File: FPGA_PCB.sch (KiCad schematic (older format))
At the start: 18 parts, among them J1 M3498-99, J10 Conn_Coaxial, J11 Conn_Coaxial, J12 Conn_01x03_Male, J13 Conn_01x03_Male, J2 M3498-99, J3 M3498-99, J4 M3498-99, J5 Conn_01x04_Male, J6 Conn_01x04_Male, J7 Conn_01x04_Male, J8 Conn_01x04_Male, J9 Conn_01x04_Male, SW1 SW_Push, U1 CPG08462

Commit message: Add files via upload
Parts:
- J1, J2, J3, J4: symbol M3498-99:M3498-99 -> FPGA_PCB-rescue:M3498-99-M3498-99
- SW1: footprint (none) -> Button_Switch_SMD:SW_SPST_TL3305A; Digikey link (none) -> https://www.digikey.com/en/products/detail/e-switch/TL3305A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
- U1: footprint (none) -> 18726-PCB-master:CPG08462_original
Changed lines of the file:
@@
 EESchema Schematic File Version 4
-LIBS:FPGA_PCB-cache
 EELAYER 30 0
 EELAYER END
@@
 F 0 "U1" H 3850 3750 60  0000 L CNN
 F 1 "CPG08462" H 3850 3650 60  0000 L CNN
-F 2 "" H 3750 3700 60  0000 C CNN
+F 2 "18726-PCB-master:CPG08462_original" H 3750 3700 60  0000 C CNN
 F 3 "" H 3750 3700 60  0000 C CNN
 	1    3750 3600
@@
 VSS
 $Comp
-L M3498-99:M3498-99 J1
+L FPGA_PCB-rescue:M3498-99-M3498-99 J1
 U 1 1 6165D330
 P 4000 6300
@@
 $EndComp
 $Comp
-L M3498-99:M3498-99 J3
+L FPGA_PCB-rescue:M3498-99-M3498-99 J3
 U 1 1 6165F6EF
 P 5950 6300
@@
 $EndComp
 $Comp
-L M3498-99:M3498-99 J4
+L FPGA_PCB-rescue:M3498-99-M3498-99 J4
 U 1 1 6166863E
 P 5950 7250
@@
 F 0 "SW1" H 10200 4685 50  0000 C CNN
 F 1 "SW_Push" H 10200 4594 50  0000 C CNN
-F 2 "" H 10200 4600 50  0001 C CNN
+F 2 "Button_Switch_SMD:SW_SPST_TL3305A" H 10200 4600 50  0001 C CNN
 F 3 "~" H 10200 4600 50  0001 C CNN
+F 4 "https://www.digikey.com/en/products/detail/e-switch/TL3305AF260QG/5816184" H 10200 4400 50  0001 C CNN "Digikey link"
 	1    10200 4400
 	1    0    0    -1
@@
 	3500 7250 4000 7250
 $Comp
-L M3498-99:M3498-99 J2
+L FPGA_PCB-rescue:M3498-99-M3498-99 J2
 U 1 1 6166408E
 P 4000 7250

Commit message: sch done
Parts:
- removed J1, J2, J3, J4: M3498-99, M3498-99:M3498-99, symbol FPGA_PCB-rescue:M3498-99-M3498-99
- added J1, J14, J15, J18, J19, J2: Conn_01x01_Male, Connector_PinHeader_2.54mm:PinHeader_1x01_P2.54mm_Vertical, symbol Connector:Conn_01x01_Male
- added J16, J17, J3, J4: 73096-2, 73096-2:73096-2, symbol 73096-2:73096-2
- added J20: Conn_01x01_Male, symbol Connector:Conn_01x01_Male
- J12, J13: footprint (none) -> Connector_PinHeader_2.54mm:PinHeader_1x03_P2.54mm_Vertical
- J5, J6, J7, J8, J9: footprint (none) -> Connector_PinHeader_2.54mm:PinHeader_1x04_P2.54mm_Vertical
- R1: footprint (none) -> Resistor_SMD:R_0805_2012Metric_Pad1.15x1.40mm_HandSolder
- U1: footprint 18726-PCB-master:CPG08462_original -> CPG08462:CPG08462_original; symbol FPGA_PCB-rescue:CPG08462-cpg08462 -> CPG08462:CPG08462
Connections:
- wire segments 139 -> 142
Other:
- note added: "in case banana jack is not working"
- moved on the sheet: C1, C2

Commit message: layout done
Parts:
- added H1, H2, H3, H4: MountingHole, MountingHole:MountingHole_3.2mm_M3, symbol Mechanical:MountingHole
- J20: footprint (none) -> Connector_PinHeader_2.54mm:PinHeader_1x01_P2.54mm_Vertical
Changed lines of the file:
@@
 F 0 "J20" H 9758 5181 50  0000 C CNN
 F 1 "Conn_01x01_Male" H 9758 5090 50  0000 C CNN
-F 2 "" H 9650 5000 50  0001 C CNN
+F 2 "Connector_PinHeader_2.54mm:PinHeader_1x01_P2.54mm_Vertical" H 9650 5000 50  0001 C CNN
 F 3 "~" H 9650 5000 50  0001 C CNN
 	1    9650 5000
@@
 Text Label 10200 5000 0    50   ~ 0
 RST
+$Comp
+L Mechanical:MountingHole H1
+U 1 1 615A752D
+P 5600 950
+F 0 "H1" H 5700 996 50  0000 L CNN
+F 1 "MountingHole" H 5700 905 50  0000 L CNN
+F 2 "MountingHole:MountingHole_3.2mm_M3" H 5600 950 50  0001 C CNN
+F 3 "~" H 5600 950 50  0001 C CNN
+	1    5600 950
+	1    0    0    -1
+$EndComp
+$Comp
+L Mechanical:MountingHole H2
+U 1 1 615A7BC1
+P 5600 1300
+F 0 "H2" H 5700 1346 50  0000 L CNN
+F 1 "MountingHole" H 5700 1255 50  0000 L CNN
+F 2 "MountingHole:MountingHole_3.2mm_M3" H 5600 1300 50  0001 C CNN
+F 3 "~" H 5600 1300 50  0001 C CNN
+	1    5600 1300
+	1    0    0    -1
+$EndComp
+$Comp
+L Mechanical:MountingHole H3
+U 1 1 615AD8DC
+P 6500 950
+F 0 "H3" H 6600 996 50  0000 L CNN
+F 1 "MountingHole" H 6600 905 50  0000 L CNN
+F 2 "MountingHole:MountingHole_3.2mm_M3" H 6500 950 50  0001 C CNN
+F 3 "~" H 6500 950 50  0001 C CNN
+	1    6500 950
+	1    0    0    -1
+$EndComp
+$Comp
+L Mechanical:MountingHole H4
+U 1 1 615B3580
+P 6500 1300
+F 0 "H4" H 6600 1346 50  0000 L CNN
+F 1 "MountingHole" H 6600 1255 50  0000 L CNN
+F 2 "MountingHole:MountingHole_3.2mm_M3" H 6500 1300 50  0001 C CNN
+F 3 "~" H 6500 1300 50  0001 C CNN
+	1    6500 1300
+	1    0    0    -1
+$EndComp
 $EndSCHEMATC

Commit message: ver 2.0
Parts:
- removed J16, J17, J3, J4: 73096-2, 73096-2:73096-2, symbol 73096-2:73096-2
- added C10, C11, C12, C13, C14, C15, C16, C17, C18, C3, C4, C5, C6, C7, C8, C9: 100p, Capacitor_SMD:C_0805_2012Metric_Pad1.15x1.40mm_HandSolder, symbol Device:C
- added J16, J17, J21, J22, J23: Conn_01x04_Male, Connector_PinHeader_2.54mm:PinHeader_1x04_P2.54mm_Vertical, symbol Connector:Conn_01x04_Male
- added J24, J25: Conn_01x01_Male, Connector_PinHeader_2.54mm:PinHeader_1x01_P2.54mm_Vertical, symbol Connector:Conn_01x01_Male
- added J26, J27: Conn_01x03_Male, Connector_PinHeader_2.54mm:PinHeader_1x03_P2.54mm_Vertical, symbol Connector:Conn_01x03_Male
- added J28, J3, J4: Conn_Coaxial, Connector_Coaxial:BNC_TEConnectivity_1478204_Vertical, symbol Connector:Conn_Coaxial
- added JP1, JP2: Jumper_NC_Dual, Connector_PinHeader_2.54mm:PinHeader_1x03_P2.54mm_Vertical, symbol Device:Jumper_NC_Dual
- added U2, U3: SN74LVC8T245DWR, SOIC127P1030X265-24N, symbol SN74LVC8T245DWR:SN74LVC8T245DWR
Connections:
- net labels added: 3.3V, clb_scan_en_3.3, clb_scan_in_3.3, clb_scan_out_3.3, conn_scan_en_3.3, conn_scan_in_3.3, conn_scan_out_3.3
- wire segments 142 -> 269
- no-connect marks 47 -> 67
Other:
- note removed: "in case banana jack is not working"
- moved on the sheet: C1, C2, J1, J12, J13, J14, J2, J20, J5, J6, J7, J8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

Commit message: ver 3.0: added i/o level shifters
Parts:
- added JP7: Jumper_NC_Dual, Connector_PinHeader_2.54mm:PinHeader_1x03_P2.54mm_Vertical, symbol Device:Jumper_NC_Dual
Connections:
- net labels added: RST_header, RST_switch
- wire segments 269 -> 275
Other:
- moved on the sheet: C1, C10, C11, C12, C13, C14, C15, C16, C17, C18, C2, C3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

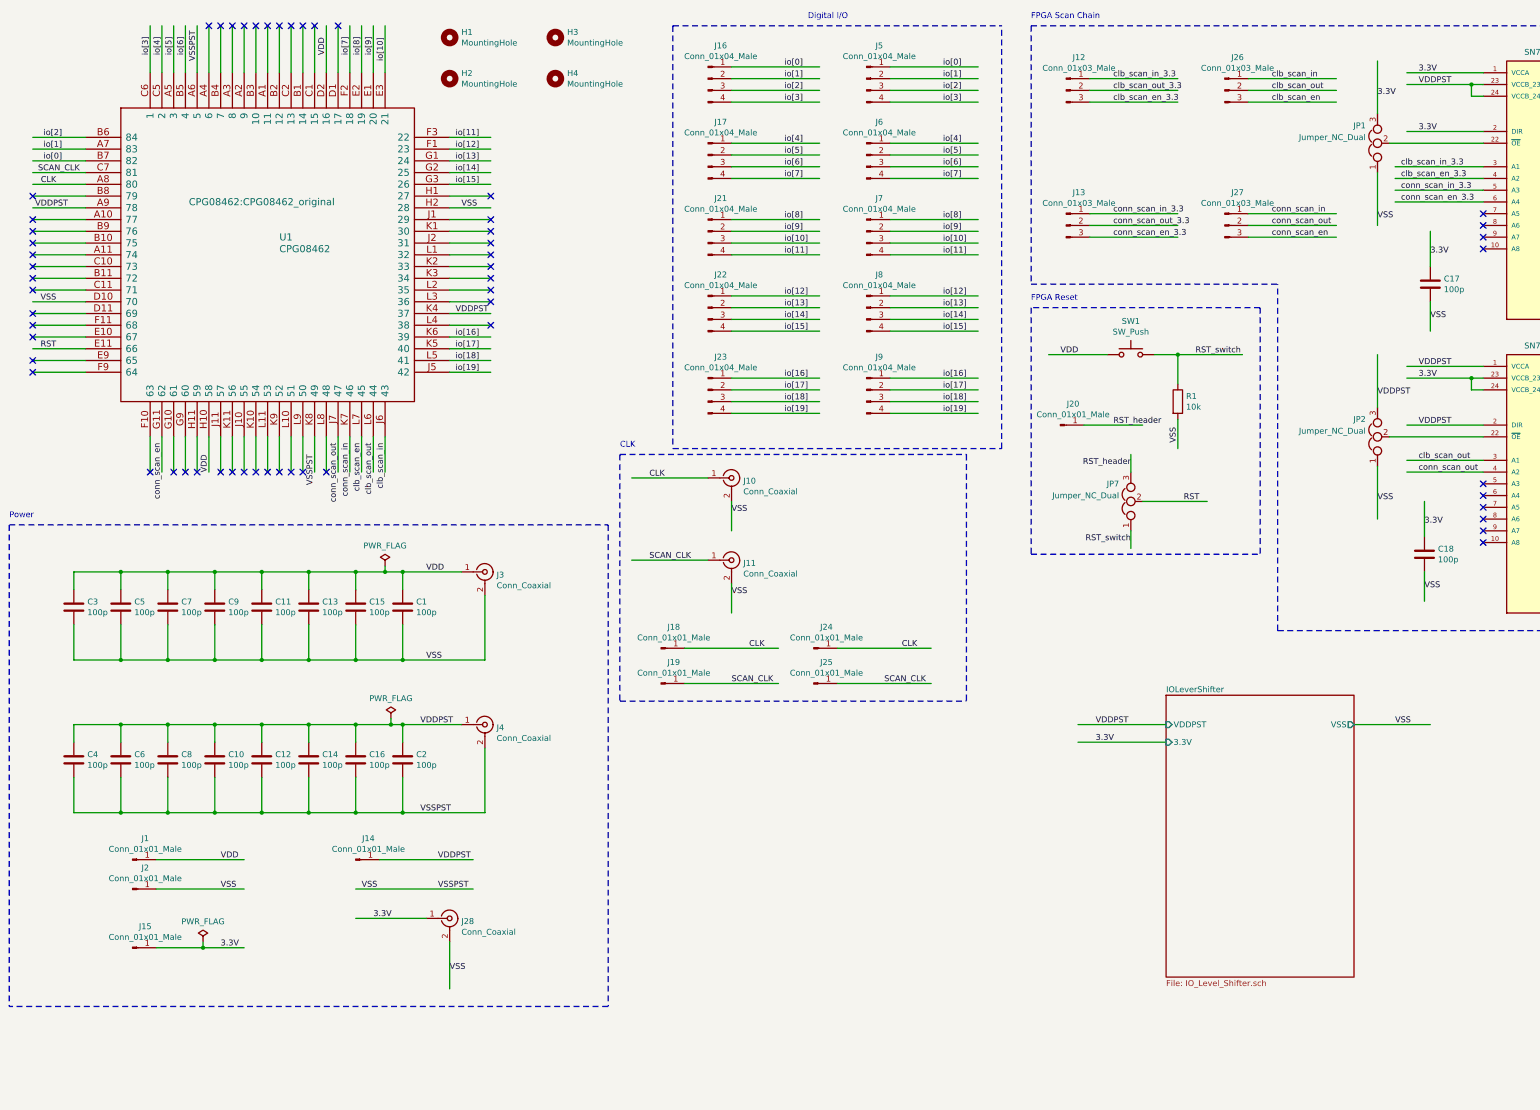
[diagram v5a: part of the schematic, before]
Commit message: ver 4.0: added 1.8V pin
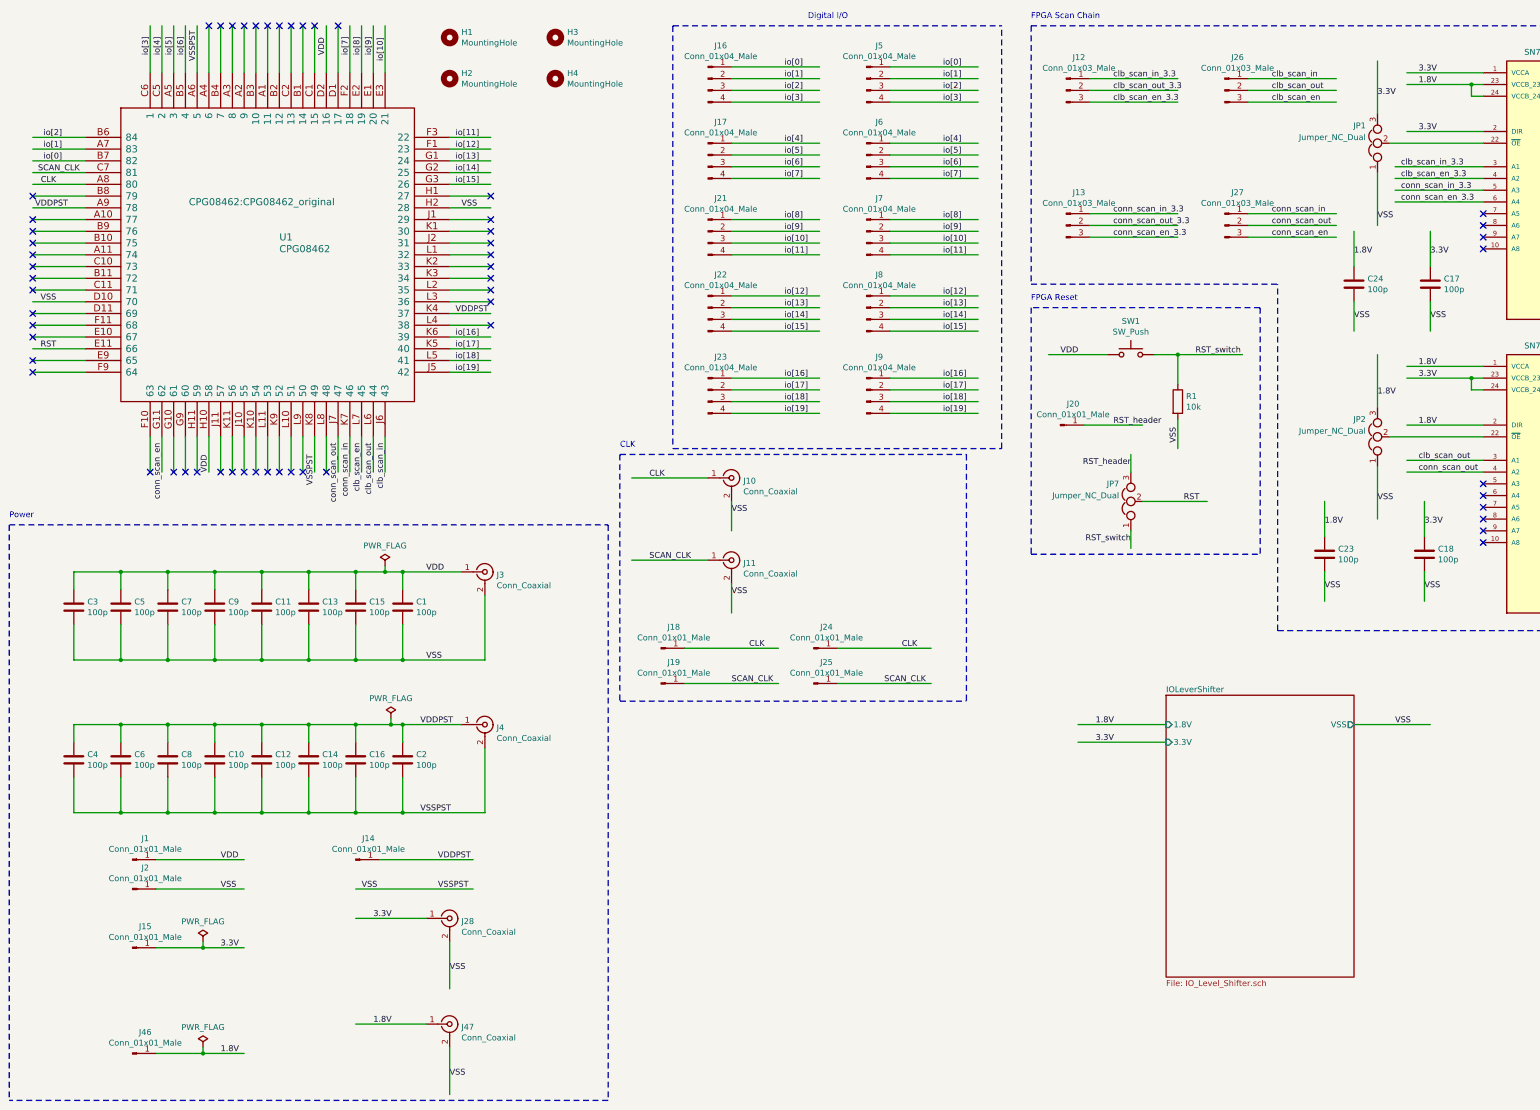
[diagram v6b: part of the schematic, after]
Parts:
- added C23, C24: 100p, Capacitor_SMD:C_0805_2012Metric_Pad1.15x1.40mm_HandSolder, symbol Device:C
- added J46: Conn_01x01_Male, Connector_PinHeader_2.54mm:PinHeader_1x01_P2.54mm_Vertical, symbol Connector:Conn_01x01_Male
- added J47: Conn_Coaxial, Connector_Coaxial:BNC_TEConnectivity_1478204_Vertical, symbol Connector:Conn_Coaxial
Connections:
- net labels added: 1.8V
- wire segments 275 -> 284
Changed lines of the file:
@@
 	15250 5600 14600 5600
 Text Label 12650 1200 0    50   ~ 0
-VDDPST
+1.8V
 Text Label 12650 1100 0    50   ~ 0
 3.3V
@@
 VSS
 Text Label 12650 3600 0    50   ~ 0
-VDDPST
+1.8V
 Text Label 12650 3700 0    50   ~ 0
 3.3V
 Text Label 12650 4100 0    50   ~ 0
-VDDPST
+1.8V
 Text Label 14850 5400 0    50   ~ 0
 VSS
@@
 Connection ~ 2400 5350
 Wire Notes Line
-	5750 9050 650  9050
+	5750 9850 650  9850
 Wire Notes Line
 	650  4950 5750 4950
@@
 	12300 3950 12300 3500
 Text Label 12300 3850 0    50   ~ 0
-VDDPST
+1.8V
 Wire Wire Line
 	12400 4200 13200 4200
@@
 Wire Wire Line
 	1900 8550 2300 8550
-Wire Notes Line
-	5750 4950 5750 9050
-Wire Notes Line
-	650  4950 650  9050
 Wire Wire Line
 	2300 8550 2300 8500
@@
 F0 "IOLeverShifter" 50
 F1 "IO_Level_Shifter.sch" 50
-F2 "VDDPST" I L 10500 6650 50
+F2 "1.8V" I L 10500 6650 50
 F3 "3.3V" I L 10500 6800 50
 F4 "VSS" O R 12100 6650 50
@@
 	9350 3100 9350 5200
 Text Label 9900 6650 0    50   ~ 0
-VDDPST
+1.8V
 Text Label 9900 6800 0    50   ~ 0
 3.3V
 Text Label 12450 6650 0    50   ~ 0
 VSS
+$Comp
+L Connector:Conn_01x01_Male J46
+U 1 1 616A5AFE
+P 1700 9450
+F 0 "J46" H 1808 9631 50  0000 C CNN
+F 1 "Conn_01x01_Male" H 1808 9540 50  0000 C CNN
+F 2 "Connector_PinHeader_2.54mm:PinHeader_1x01_P2.54mm_Vertical" H 1700 9450 50  0001 C CNN
+F 3 "~" H 1700 9450 50  0001 C CNN
+	1    1700 9450
+	1    0    0    -1
+$EndComp
+Text Label 2450 9450 0    50   ~ 0
+1.8V
+$Comp
+L Connector:Conn_Coaxial J47
+U 1 1 616A5B09
+P 4400 9200
+F 0 "J47" H 4500 9175 50  0000 L CNN
+F 1 "Conn_Coaxial" H 4500 9084 50  0000 L CNN
+F 2 "Connector_Coaxial:BNC_TEConnectivity_1478204_Vertical" H 4400 9200 50  0001 C CNN
+F 3 " ~" H 4400 9200 50  0001 C CNN
+	1    4400 9200
+	1    0    0    -1
+$EndComp
+Wire Wire Line
+	4200 9200 3600 9200
+Wire Wire Line
+	4400 9400 4400 9800
+Text Label 3750 9200 0    50   ~ 0
+1.8V
+Text Label 4400 9650 0    50   ~ 0
+VSS
+Wire Wire Line
+	1900 9450 2300 9450
+Wire Wire Line
+	2300 9450 2300 9400
+$Comp
+L power:PWR_FLAG #FLG0104
+U 1 1 616A5B19
+P 2300 9400
+F 0 "#FLG0104" H 2300 9475 50  0001 C CNN
+F 1 "PWR_FLAG" H 2300 9573 50  0000 C CNN
+F 2 "" H 2300 9400 50  0001 C CNN
+F 3 "~" H 2300 9400 50  0001 C CNN
+	1    2300 9400
+	1    0    0    -1
+$EndComp
+Connection ~ 2300 9450
+Wire Wire Line
+	2300 9450 2650 9450
+Wire Notes Line
+	650  4950 650  9850
+Wire Notes Line
+	5750 4950 5750 9850
+Wire Wire Line
+	11850 5050 11850 4750
+Wire Wire Line
+	11850 5350 11850 5600
+Text Label 11850 4950 0    50   ~ 0
+1.8V
+Text Label 11850 5500 0    50   ~ 0
+VSS
+$Comp
+L Device:C C23
+U 1 1 6173A5CC
+P 11850 5200
+F 0 "C23" H 11965 5246 50  0000 L CNN
+F 1 "100p" H 11965 5155 50  0000 L CNN
+F 2 "Capacitor_SMD:C_0805_2012Metric_Pad1.15x1.40mm_HandSolder" H 11888 5050 50  0001 C CNN
+F 3 "~" H 11850 5200 50  0001 C CNN
+	1    11850 5200
+	1    0    0    -1
+$EndComp
+Wire Wire Line
+	12100 2750 12100 2450
+Wire Wire Line
+	12100 3050 12100 3300
+Text Label 12100 2650 0    50   ~ 0
+1.8V
+Text Label 12100 3200 0    50   ~ 0
+VSS
+$Comp
+L Device:C C24
+U 1 1 61752167
+P 12100 2900
+F 0 "C24" H 12215 2946 50  0000 L CNN
+F 1 "100p" H 12215 2855 50  0000 L CNN
+F 2 "Capacitor_SMD:C_0805_2012Metric_Pad1.15x1.40mm_HandSolder" H 12138 2750 50  0001 C CNN
+F 3 "~" H 12100 2900 50  0001 C CNN
+	1    12100 2900
+	1    0    0    -1
+$EndComp
 $EndSCHEMATC
